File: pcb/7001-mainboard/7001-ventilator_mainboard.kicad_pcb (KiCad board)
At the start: 2 copper layers, 98.5 x 110 mm, 153 parts, among them J1 USB_B_Micro, J10 6-pin header, J11 4-pin screw terminal, J12 3-pin screw terminal, J13 2-pin screw terminal, J14 2-pin screw terminal, J15 2x10-pin header, J16 10-pin SWD header, J2 4-pin header, J3 2-pin screw terminal, J4 DNI, J5 2-pin screw terminal, J6 5V out, J7 2-pin screw terminal, J8 3-pin screw terminal, J9 Raspberry_Pi_2_3, U1 MPRLS0001PG0000SA, U10 ABPMAND001PG2A3, U11 MPVZ5010GW6U, U12 MPVZ5010GW6U, U13 ITS4142NHUMA1, U14 ITS4142NHUMA1, U2 TPD2E2U06, U3 LPC11U37FBD48-401_, U4 MCP1825S-3302E, U5 S24SE05004PDFA_DC-DC, U6 LM2937IMP-12/NOPB, U7 AD5410AREZ, U8 MPRLS0001PG0000SA, U9 ABPMAND001PG2A3, Y1 12MHz

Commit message: PCB: schematics for V2
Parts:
- removed J12: 3-pin screw terminal, Jitter_Footprints:TerminalBlock_Wurth_WR-TBL_691322110003_1x03_P3.50mm_Horizontal
- removed JP1: 5V_jumper, Connector_PinHeader_2.54mm:PinHeader_1x03_P2.54mm_Vertical
- removed R22, R23, R27, R28: 0, Resistor_SMD:R_0805_2012Metric
- removed R24, R25, R26: DNI, Resistor_SMD:R_0805_2012Metric
- removed U10: ABPMAND001PG2A3, Jitter_Footprints:ABPM+DXXX000XX0XX
- removed U12: MPVZ5010GW6U, Jitter_Footprints:MPVZ5010GW6U
- added FB1: BLM18HE601SN1D, Inductor_SMD:L_0603_1608Metric, F.Cu at (118.8, 123.8)
- added FB2: BLM18HE601SN1D, Inductor_SMD:L_0603_1608Metric, F.Cu at (102.2, 109.3)
- added H7: DNI (mounting hole), MountingHole:MountingHole_3.5mm_Pad_Via, F.Cu at (71.0, 159.0)
- added Q1: NX3020NAKV,115, Package_TO_SOT_SMD:SOT-666, F.Cu at (238.0, 176.2)
- added R44: 3.3k, Resistor_SMD:R_0805_2012Metric, F.Cu at (224.4, 181.0)
- added R45: 3.3k, Resistor_SMD:R_0805_2012Metric, F.Cu at (236.5, 170.2)
- added R46: 3.3k, Resistor_SMD:R_0805_2012Metric, F.Cu at (240.9, 167.1)
- added R47: 150, Resistor_SMD:R_0805_2012Metric, F.Cu at (117.5, 119.7)
- added R48: 2.2k, Resistor_SMD:R_0805_2012Metric, F.Cu at (119.5, 119.8)
- added R49: 150, Resistor_SMD:R_0805_2012Metric, F.Cu at (102.5, 113.5)
- added R50: 150, Resistor_SMD:R_0805_2012Metric, F.Cu at (102.5, 111.4)
- added TP6: DNI, TestPoint:TestPoint_THTPad_D1.5mm_Drill0.7mm, F.Cu at (242.2, 173.3)
- added TP7: DNI, TestPoint:TestPoint_THTPad_D1.5mm_Drill0.7mm, F.Cu at (130.5, 199.0)
- added U15: MCP4725, Package_TO_SOT_SMD:SOT-23-6, F.Cu at (122.2, 195.5)
- added U16: LD1086DT33TR, Package_TO_SOT_SMD:TO-252-2, F.Cu at (112.8, 123.5)
- C14: value 10uF -> 10uF 50V; footprint Capacitor_SMD:C_0805_2012Metric -> Capacitor_SMD:C_1210_3225Metric
- C20: value 100nF 50V -> 2.2nF
- C21: value 10uF 50V -> 100nF; footprint Capacitor_SMD:C_1210_3225Metric -> Capacitor_SMD:C_0805_2012Metric
- C23: value 10nF -> 100nF
- C24, C41: value 100nF 50V -> 10uF 50V; footprint Capacitor_SMD:C_0805_2012Metric -> Capacitor_SMD:C_1210_3225Metric
- C26: value 100nF -> 10uF 50V; footprint Capacitor_SMD:C_0805_2012Metric -> Capacitor_SMD:C_1210_3225Metric
- C27: value 10nF -> 2.2nF 50V
- C36: value 470pF -> 1nF
- C40: value 100nF -> 2.2nF
- C43: value 100nF -> 10uF
- C48: value 10nF -> 100nF 50V
- D11: value D_TVS -> D_Schottky; footprint Jitter_Footprints:WE-TVSP_TVS_DIODE -> Diode_SMD:D_SOD-123F
- D5: value D_TVS -> Green; footprint Jitter_Footprints:WE-TVSP_TVS_DIODE -> LED_SMD:LED_0805_2012Metric
- J11: value 4-pin screw terminal -> 2-pin screw terminal
- J2: value 4-pin header -> 2-pin screw terminal; footprint Connector_PinSocket_2.54mm:PinSocket_1x04_P2.54mm_Vertical -> Jitter_Footprints:TerminalBlock_Wurth_WR-TBL_691322110002_1x02_P3.50mm_Horizontal
- J4: value DNI -> 2-pin screw terminal; footprint Connector_PinHeader_2.54mm:PinHeader_1x03_P2.54mm_Vertical -> Jitter_Footprints:TerminalBlock_Wurth_WR-TBL_691322110002_1x02_P3.50mm_Horizontal
- J6: footprint Connector_PinHeader_2.54mm:PinHeader_1x02_P2.54mm_Vertical -> Connector_PinHeader_2.54mm:PinHeader_1x05_P2.54mm_Vertical
- J7: value 2-pin screw terminal -> 6-pin FFC connector; footprint Jitter_Footprints:TerminalBlock_Wurth_WR-TBL_691322110002_1x02_P3.50mm_Horizontal -> Jitter_Footprints:Hirose_FH12-6S-0.5SH_1x06-1MP_P0.50mm_Horizontal
- J8: value 3-pin screw terminal -> 2-pin screw terminal; footprint Jitter_Footprints:TerminalBlock_Wurth_WR-TBL_691322110003_1x03_P3.50mm_Horizontal -> Jitter_Footprints:TerminalBlock_Wurth_WR-TBL_691322110004_1x04_P3.50mm_Horizontal
- R10: value 10k -> 68k
- R11: value 0 -> 1k5
- R12: value 10k -> 1k5
- R13, R33: value 0 -> 100k
- R14: value DNI -> 100k
- R15: value 150 -> 10k
- R18: value 0 -> 10k
- R19, R37: value DNI -> 3.3k
- R21: value 100k -> 4.7k
- R31: value 3.3k -> 68k
- R32: value 10k -> 4.7k
- R35: value 4.7k -> 10k
- R8, R9: value 1k5 -> 0
- U6: value LM2937IMP-12/NOPB -> MCP4725; footprint Package_TO_SOT_SMD:SOT-223-3_TabPin2 -> Package_TO_SOT_SMD:SOT-23-6
- U7: value AD5410AREZ -> ITS4142NHUMA1; footprint Jitter_Footprints:TSSOP-24-1EP_4.4x7.8mm_P0.65mm -> Package_TO_SOT_SMD:SOT-223
- U9: value ABPMAND001PG2A3 -> ABPDXXX000XXAX5; footprint Jitter_Footprints:ABPM+DXXX000XX0XX -> Jitter_Footprints:ABPDXXX000XX0XX
- moved R12 165.1 mm to (232.1, 170.5), turned to 0 degrees
- moved R11 154.5 mm to (236.5, 167.2), turned to 0 degrees
- moved R9 153.7 mm to (233.8, 173.4), turned to 0 degrees
- moved R15 151.4 mm to (220.0, 179.8), turned to 0 degrees
- moved R8 147.1 mm to (229.4, 173.4), turned to 0 degrees
- moved R14 145.7 mm to (215.1, 187.4)
- moved C24 144.1 mm to (227.9, 160.6), turned to 0 degrees
- moved C21 142.0 mm to (225.0, 172.2), turned to 0 degrees
- moved C1 134.8 mm to (241.6, 162.9)
- moved R35 134.1 mm to (229.4, 176.4), turned to 0 degrees
- moved R18 132.9 mm to (215.1, 184.5), turned to 0 degrees
- moved C20 132.1 mm to (220.0, 182.8)
- moved R10 128.8 mm to (225.0, 178.1), turned to 0 degrees
- moved R37 127.2 mm to (215.1, 190.4)
- moved C15 124.9 mm to (219.5, 185.7), turned to 0 degrees
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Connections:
- net /24V_SW1_OUT renamed /EXHALE_VALVE
- net /24V_SW2_OUT renamed /INHALE_VALVE
- net /pressure_sensor/MPVZ5010_1_OUT renamed /pressure_sensor/MPVZ5010_OUT
- net /switch_1_out renamed /EXHALE_PWM
- net /switch_2_out renamed /INHALE_PWM
- C1 pad 1: /USB_VBUS -> +5V
- C11 pad 1: /DCDC_5V -> +5V
- C14 pad 1: +3V3 -> +24V
- C15 pad 1: +3V3 -> /POWER_STATUS
- C16 pad 1: /DCDC_5V -> +5V
- C19 pad 1: +24V -> Net-(C19-Pad1)
- C20 pad 1: +24V -> /A_MFC_FEEDBACK_O2
- C21 pad 1: +24V -> /USER_SWITCH
- C23 pad 1: +24V -> +5V
- C23 pad 2: Net-(C23-Pad2) -> GND
- C26 pad 1: Net-(C26-Pad1) -> +24V
- C27 pad 1: /A_PREG_PRESSURE -> /EXTRA_VALVE
- C35 pad 1: /A_PRESSURE_1 -> /A_PSENSE_3
- C36 pad 1: /pressure_sensor/MPVZ5010_2_OUT -> Net-(C36-Pad1)
- C37 pad 1: /A_PRESSURE_2 -> /A_MFC_PRESSURE
- C38 pad 1: +12V -> /V_flow_heater
- C39 pad 1: +12V -> /V_flow_heater
- C40 pad 1: +5V -> /A_MFC_FEEDBACK_AIR
- C41 pad 1: +12V -> +24V
- C43 pad 1: /A_FLOW -> +3V3
- C48 pad 1: +24V -> /V_flow_3v3
- C48 pad 2: Net-(C48-Pad2) -> GND
- D11 pad 1: GND -> /EXTRA_VALVE
- D11 pad 2: +24V -> GND
- D5 pad 2: /I_PREG_SETPOINT -> Net-(D5-Pad2)
- FL1 pad 1: Net-(C46-Pad1) -> Net-(C46-Pad2)
- FL1 pad 2: Net-(C46-Pad2) -> Net-(C46-Pad1)
- FL1 pad 3: Net-(C47-Pad1) -> GND
- FL1 pad 4: GND -> Net-(C47-Pad1)
- J11 pad 2: +5V -> Net-(J11-Pad2)
- J11 pad 3: /I2C_SDA -> /MFC_SETPOINT_AIR
- J11 pad 4: /I2C_SCL -> +24V
- J15 pad 2: /RPI_IO_3 -> /RPI_IO_2
- J15 pad 4: /RPI_IO_2 -> /RPI_IO_1
- J15 pad 6: /RPI_IO_1 -> /~ISP~
- J2 pad 1: GND -> Net-(J2-Pad1)
- J2 pad 2: /SWCLK -> Net-(J2-Pad2)
- J3 pad 2: +12V -> Net-(J3-Pad2)
- J4 pad 2: /~RESET~ -> /EXTRA_VALVE
- J5 pad 1: Net-(C46-Pad1) -> Net-(C46-Pad2)
- J5 pad 2: Net-(C46-Pad2) -> Net-(C46-Pad1)
- J6 pad 2: +5V -> (no net)
- J7 pad 1: GND -> /V_flow_3v3
- J7 pad 2: +24V -> GND
- J8 pad 2: /I_PREG_FEEDBACK -> Net-(J8-Pad2)
- J8 pad 3: /I_PREG_SETPOINT -> /MFC_SETPOINT_O2
- J9 pad 11: (no net) -> /RPI_~ISP~
- J9 pad 36: /~RESET~ -> /RPI_~RST~
- J9 pad 40: /RPI_IO_3 -> (no net)
- J9 pad 5: (no net) -> /RPI_ON_OFF
- R1 pad 1: /A_PRESSURE_1 -> /A_PSENSE_3
- R10 pad 1: /PREG_OK -> /A_MFC_FEEDBACK_O2
- R10 pad 2: +3V3 -> Net-(J8-Pad2)
- R11 pad 1: GND -> Net-(J2-Pad2)
- R11 pad 2: Net-(R11-Pad2) -> +3V3
- R12 pad 1: /A_PREG_PRESSURE -> Net-(J2-Pad1)
- R12 pad 2: Net-(R12-Pad2) -> /POWER_STATUS
- R13 pad 1: Net-(R12-Pad2) -> GND
- R13 pad 2: /I_PREG_FEEDBACK -> /A_MFC_PRESSURE
- R14 pad 1: /A_PREG_PRESSURE -> GND
- R14 pad 2: GND -> /A_MFC_FEEDBACK_O2
- R15 pad 1: GND -> +3V3
- R15 pad 2: Net-(R12-Pad2) -> Net-(J3-Pad2)
- R18 pad 1: +3V3 -> Net-(J3-Pad2)
- R18 pad 2: /V_PU -> /USER_SWITCH
- R19 pad 1: /V_PU -> Net-(D5-Pad2)
- R19 pad 2: +5V -> /EXTRA_VALVE
- R2 pad 1: /A_PRESSURE_2 -> /A_MFC_PRESSURE
- R2 pad 2: /pressure_sensor/MPVZ5010_2_OUT -> Net-(C36-Pad1)
- R20 pad 2: /A_PRESSURE_1 -> /A_PSENSE_3
- R21 pad 2: /A_PRESSURE_2 -> /USB_VBUS
- R31 pad 1: GND -> /A_MFC_FEEDBACK_AIR
- R31 pad 2: /A_FLOW -> Net-(J11-Pad2)
- R32 pad 1: /A_FLOW -> GND
- R32 pad 2: Net-(J12-Pad3) -> /EXTRA_PWM
- R33 pad 1: /DCDC_5V -> GND
- R33 pad 2: +5V -> /A_MFC_FEEDBACK_AIR
- R35 pad 1: GND -> /~ISP~
- R35 pad 2: /PREG_CLEAR -> +3V3
- R37 pad 1: Net-(R37-Pad1) -> /I2C_3V3_SCL
- R37 pad 2: GND -> +3V3
- R7 pad 2: /DCDC_5V -> +5V
- R8 pad 1: /I2C_SCL -> /~RESET~
- R8 pad 2: /V_PU -> /RPI_~RST~
- R9 pad 1: /I2C_SDA -> /~ISP~
- R9 pad 2: /V_PU -> /RPI_~ISP~
- TP2 pad 1: /A_PRESSURE_1 -> /A_PSENSE_3
- TP3 pad 1: /A_PRESSURE_2 -> /A_MFC_PRESSURE
- U1 pad 12: Net-(R22-Pad2) -> +3V3
- U3 pad 10: (no net) -> /LED_STATUS
- U3 pad 11: /UART_RX -> /USER_SWITCH
- U3 pad 12: /UART_TX -> /POWER_STATUS
- U3 pad 14: +3V3 -> /USB_VBUS
- U3 pad 15: /I2C_SCL -> /I2C_3V3_SCL
- U3 pad 16: /I2C_SDA -> /I2C_3V3_SDA
- U3 pad 23: /PREG_CLEAR -> /PSENSE_2_SPI_~CS~
- U3 pad 24: /PREG_OK -> (no net)
- U3 pad 25: /PREG_SPI_~CS~ -> (no net)
- U3 pad 26: /PREG_SPI_MISO -> (no net)
- U3 pad 32: /A_PREG_PRESSURE -> /A_PSENSE_3
- U3 pad 33: /A_FLOW -> /A_MFC_PRESSURE
- U3 pad 34: /A_PRESSURE_2 -> /A_MFC_FEEDBACK_AIR
- U3 pad 35: /A_PRESSURE_1 -> /A_MFC_FEEDBACK_O2
- U3 pad 36: /MCU_IO_1 -> /EXTRA_PWM
- U3 pad 38: /PREG_SPI_MOSI -> /MCU_IO_3
- U3 pad 40: /PSENSE_2_SPI_~CS~ -> /MCU_IO_1
- U3 pad 43: /PREG_SPI_CLK -> /MCU_IO_4
- U3 pad 45: /LED_STATUS -> /RPI_ON_OFF
- U3 pad 46: /MCU_IO_4 -> /UART_RX
- U3 pad 47: /MCU_IO_3 -> /UART_TX
- U3 pad 9: (no net) -> GND
- U5 pad 6: /DCDC_5V -> +5V
- U6 pad 1: +24V -> /MFC_SETPOINT_O2
- U6 pad 3: +12V -> +5V
- U7 pad 1: GND -> /EXTRA_VALVE
- U7 pad 2: +3V3 -> GND
- U7 pad 3: /PREG_OK -> /EXTRA_PWM
- U7 pad 4: GND -> +24V
- U8 pad 12: Net-(R23-Pad2) -> +3V3
- U9 pad 2: Net-(R22-Pad2) -> (no net)
- U9 pad 3: /PSENSE_1_DATA_READY -> Net-(C36-Pad1)
- U9 pad 4: Net-(U9-Pad4) -> (no net)
- U9 pad 5: /pressure_sensor/P_SDA -> (no net)
- U9 pad 6: /pressure_sensor/P_SCL -> +5V
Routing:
- net +3V3: track 295.0 -> 0.47 mm, vias 9 -> 0
- net +5V: track 255.1 -> 24.8 mm, vias 8 -> 0
- net /I2C_SDA: track 126.9 -> 0.00 mm, vias 4 -> 0
- net /I2C_SCL: track 126.4 -> 0.00 mm, vias 6 -> 0
- net +24V: track 163.9 -> 49.7 mm
- net /A_PREG_PRESSURE: track 102.0 -> 0.00 mm, vias 2 -> 0
- net GND: track 271.6 -> 170.9 mm, vias 166 -> 48
- net /PSENSE_SPI_MISO: track 99.7 -> 0.00 mm, vias 6 -> 0
- net /EXHALE_PWM: track 96.0 -> 3.03 mm, vias 4 -> 0
- net /~RESET~: track 91.5 -> 0.00 mm, vias 2 -> 0
- net /PSENSE_2_DATA_READY: track 87.6 -> 0.00 mm, vias 5 -> 0
- net /PSENSE_SPI_MOSI: track 87.0 -> 0.00 mm, vias 4 -> 0
- net /A_FLOW: track 86.3 -> 0.00 mm, vias 2 -> 0
- net /PSENSE_RESET: track 88.1 -> 1.97 mm, vias 4 -> 1
- net /PREG_SPI_MOSI: track 83.3 -> 0.00 mm, vias 4 -> 0
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- removed copper zone on F.Cu, net +24V
- removed copper zone on F.Cu, net +5V
- removed copper zone on F.Cu, net GND

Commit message: Update schematics (PSU connector) + BOM
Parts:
- removed J2: 2-pin screw terminal, Jitter_Footprints:TerminalBlock_Wurth_WR-TBL_691322110002_1x02_P3.50mm_Horizontal
- added C50: 100nF, Capacitor_SMD:C_0805_2012Metric, F.Cu at (191.8, 135.5)
- added R22: 1k5, Resistor_SMD:R_0805_2012Metric, F.Cu at (191.8, 138.4)
- added R23: 1k5, Resistor_SMD:R_0805_2012Metric, F.Cu at (196.2, 135.5)
- J11, J8: footprint Jitter_Footprints:TerminalBlock_Wurth_WR-TBL_691322110004_1x04_P3.50mm_Horizontal -> Jitter_Footprints:TerminalBlock_Wurth_WR-TBL_691322110005_1x05_P3.50mm_Horizontal
- J5: footprint Jitter_Footprints:TerminalBlock_Wurth_WR-TBL_691322110002_1x02_P3.50mm_Horizontal -> Jitter_Footprints:TerminalBlock_Wurth_WR-TBL_691322110008_1x08_P3.50mm_Horizontal
- moved J3 43.2 mm to (158.5, 162.5)
- moved J1 10.5 mm to (162.3, 172.2)
- moved U2 10.5 mm to (156.3, 172.4)
- moved J5 3.65 mm to (158.5, 147.0)
- moved D4 1.69 mm to (154.2, 139.5)
- moved J8 1.00 mm to (133.5, 203.5)
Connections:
- C15 pad 1: /POWER_STATUS -> /POWER_STATUS_DISCHARGING
- J11 pad 4: +24V -> GND
- J5 pad 1: Net-(C46-Pad2) -> GND
- J5 pad 2: Net-(C46-Pad1) -> GND
- J8 pad 4: +24V -> GND
- R11 pad 1: Net-(J2-Pad2) -> Net-(J5-Pad6)
- R12 pad 1: Net-(J2-Pad1) -> Net-(J5-Pad5)
- R12 pad 2: /POWER_STATUS -> /POWER_STATUS_DISCHARGING
- U3 pad 12: /POWER_STATUS -> /POWER_STATUS_FAIL
- U3 pad 13: /PSENSE_RESET -> /POWER_STATUS_DISCHARGING
- U3 pad 24: (no net) -> /PSENSE_RESET

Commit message: PCB: layout in progress
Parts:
- removed R11: 1k5, Resistor_SMD:R_0805_2012Metric
- moved R42 119.9 mm to (98.1, 173.2)
- moved R43 119.9 mm to (99.0, 178.4)
- moved D10 119.9 mm to (101.8, 178.2)
- moved D9 119.9 mm to (99.1, 175.2)
- moved C24 108.9 mm to (126.2, 199.8), turned to 180 degrees
- moved TP6 105.2 mm to (139.4, 196.2)
- moved C1 101.0 mm to (146.0, 195.6), turned to 270 degrees
- moved TP2 100.0 mm to (92.2, 150.9)
- moved R10 88.1 mm to (139.4, 199.2), turned to 270 degrees
- moved C20 84.6 mm to (136.8, 198.6), turned to 180 degrees
- moved TP5 81.3 mm to (97.3, 137.1)
- moved R41 81.3 mm to (94.8, 137.6)
- moved TP1 81.3 mm to (92.4, 137.2)
- moved D8 81.3 mm to (94.8, 141.2)
- moved R14 79.4 mm to (136.8, 200.5)
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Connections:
- J5 pad 8: Net-(J5-Pad8) -> Net-(J5-Pad6)
- J7 pad MP: (no net) -> GND
- R23 pad 1: Net-(J5-Pad8) -> Net-(J5-Pad6)
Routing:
- net +24V: track 49.7 -> 181.4 mm, vias 0 -> 2
- net +3V3: track 0.47 -> 62.2 mm
- net /I2C_3V3_SDA: track 0.00 -> 60.4 mm, vias 0 -> 2
- net /I2C_3V3_SCL: track 0.00 -> 57.4 mm, vias 0 -> 2
- net GND: track 170.9 -> 223.5 mm, vias 48 -> 71
- net Net-(J5-Pad6): track 0.00 -> 38.6 mm
- net Net-(J5-Pad7): track 0.00 -> 34.9 mm
- net /RPI_~RST~: track 51.5 -> 85.4 mm
- net Net-(J5-Pad5): track 0.00 -> 32.4 mm
- net /RPI_IO_1: track 53.7 -> 86.1 mm
- net /RPI_IO_2: track 48.4 -> 79.8 mm
- net /RPI_ON_OFF: track 32.9 -> 62.0 mm
- net /RPI_~ISP~: track 28.9 -> 55.9 mm
- net /RPI_TX: track 39.6 -> 66.2 mm
- net /RPI_RX: track 36.4 -> 62.0 mm
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- added copper zone on F.Cu, net +5V
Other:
- board size 98.5 x 110 mm -> 99 x 110.5 mm

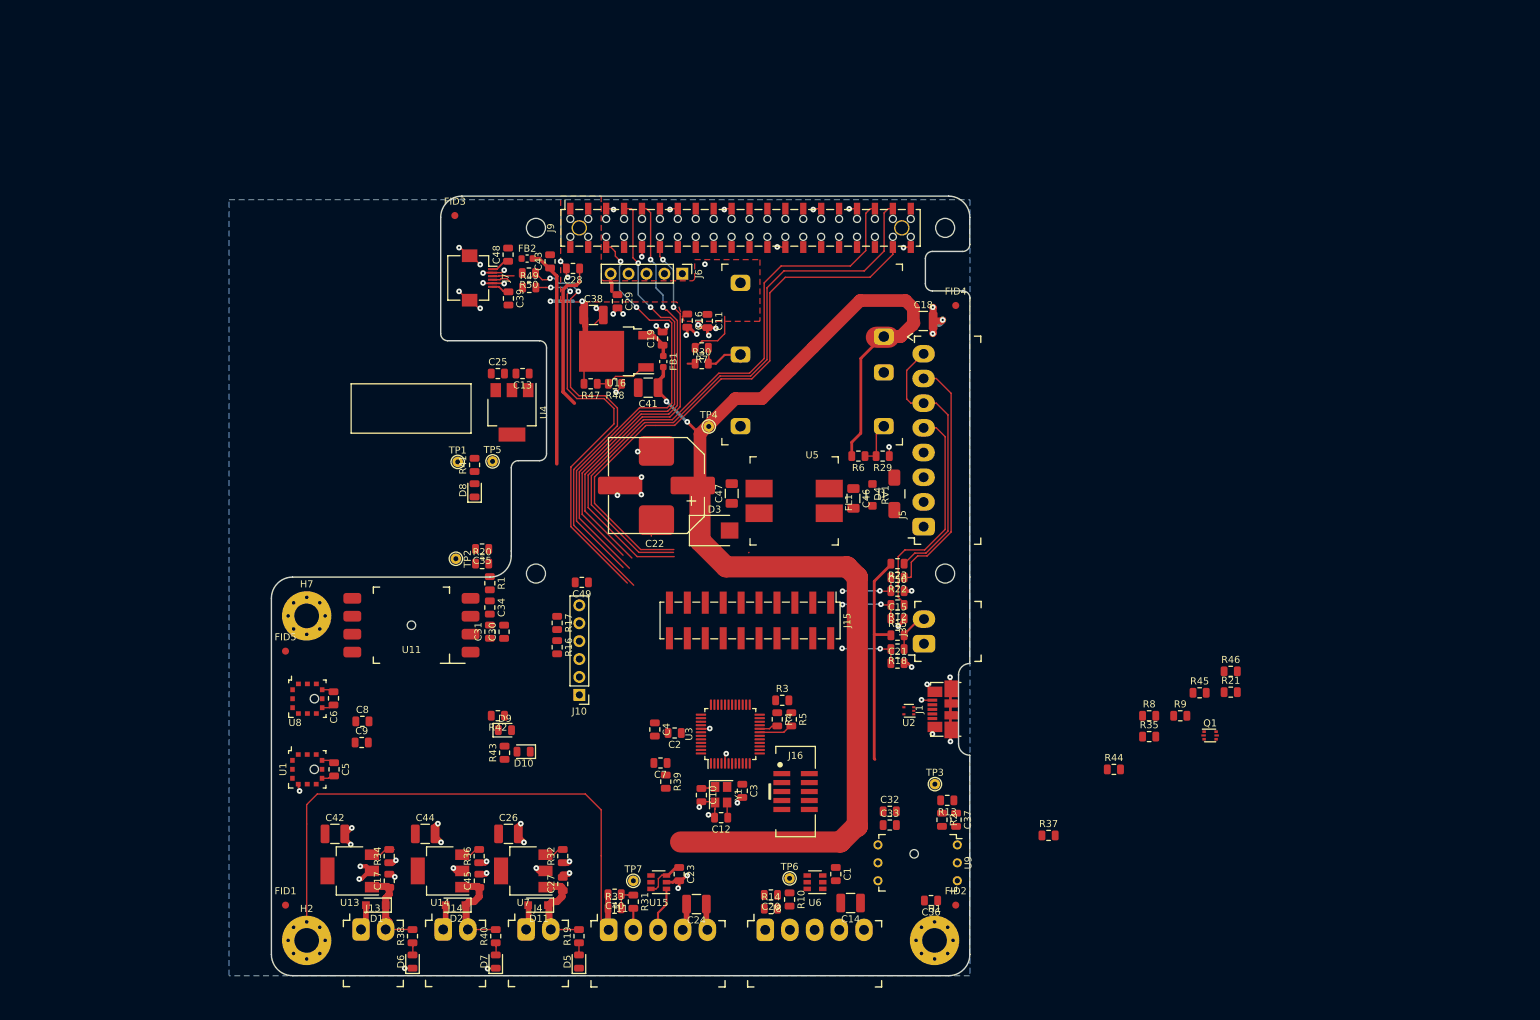
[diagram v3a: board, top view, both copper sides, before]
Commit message: PCB layout: position of components near-final
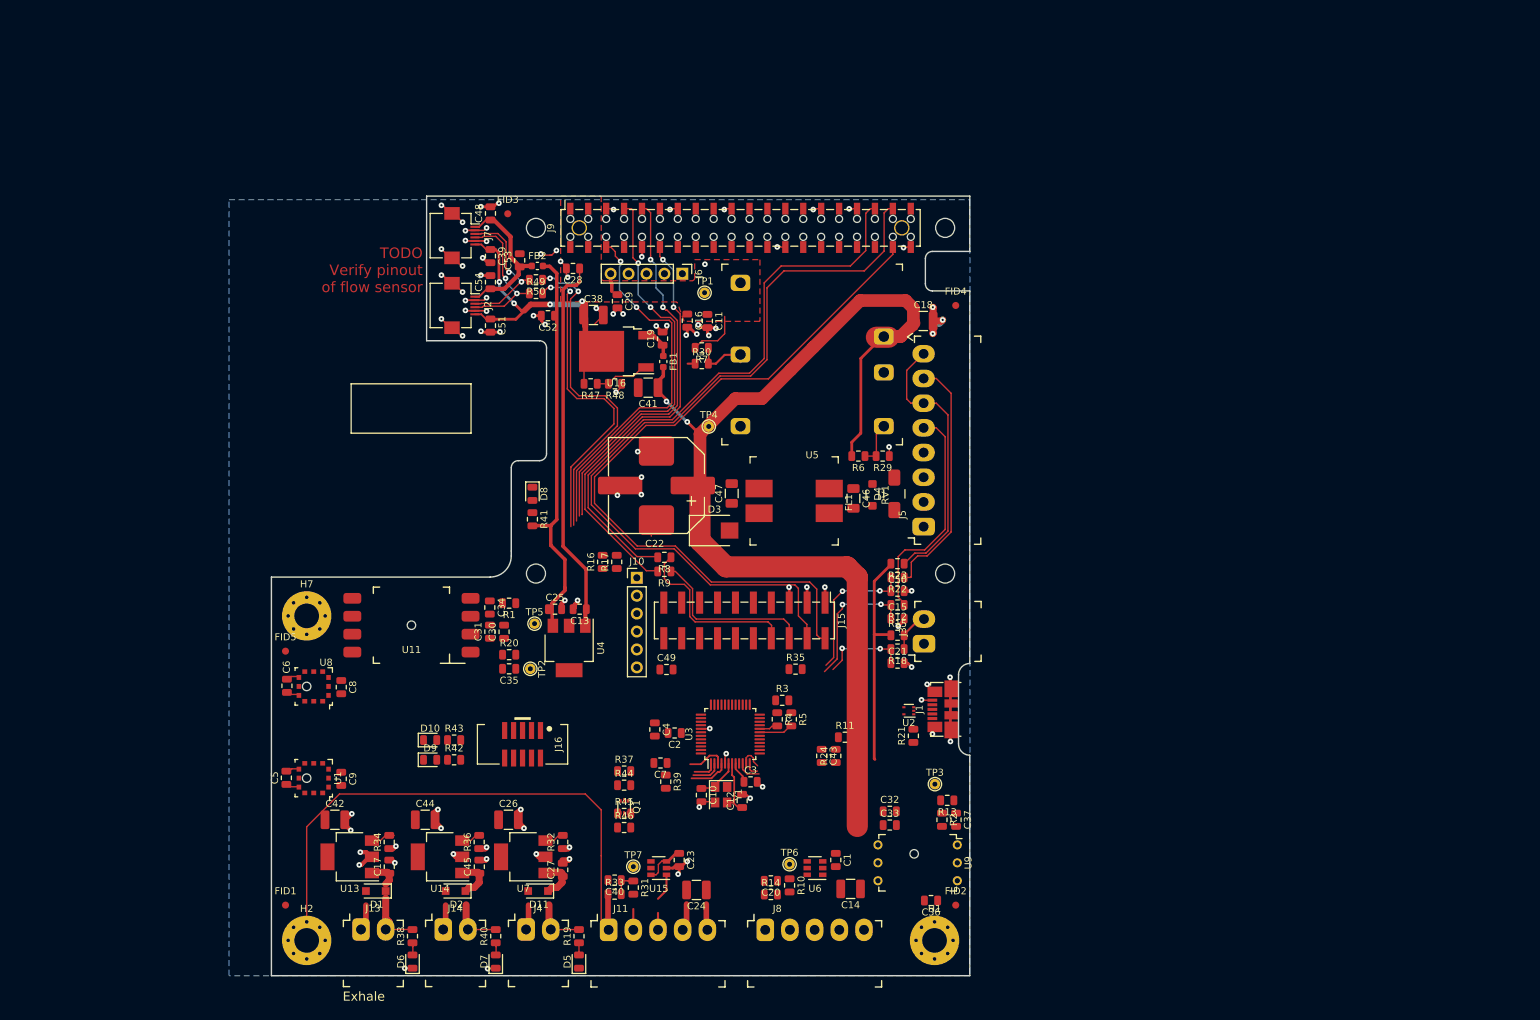
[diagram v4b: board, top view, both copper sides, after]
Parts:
- added C51: 100nF 50V, Capacitor_SMD:C_0805_2012Metric, F.Cu at (97.0, 117.8)
- added C52: 1uF, Capacitor_SMD:C_0805_2012Metric, F.Cu at (105.2, 116.5)
- added C53: 10uF, Capacitor_SMD:C_0805_2012Metric, F.Cu at (101.2, 108.6)
- added C54: 100nF 50V, Capacitor_SMD:C_0805_2012Metric, F.Cu at (97.0, 111.7)
- added J2: 6-pin FFC connector, Jitter_Footprints:Hirose_FH12-6S-0.5SH_1x06-1MP_P0.50mm_Horizontal, F.Cu at (93.0, 115.0)
- added R11: 10k, Resistor_SMD:R_0805_2012Metric, F.Cu at (147.3, 176.2)
- added R24: 1k5, Resistor_SMD:R_0805_2012Metric, F.Cu at (146.0, 178.8)
- C43: value 10uF -> 100nF
- R47: value 150 -> 150 1%
- R48: value 2.2k -> 2.32k 1%
- moved R46 88.8 mm to (116.0, 189.0)
- moved Q1 83.7 mm to (116.0, 186.1), turned to 270 degrees
- moved R45 83.3 mm to (116.0, 187.0)
- moved C43 80.0 mm to (144.0, 178.8), turned to 270 degrees
- moved R9 75.9 mm to (121.7, 152.7), turned to 180 degrees
- moved R8 72.3 mm to (121.7, 150.7), turned to 180 degrees
- moved R44 69.5 mm to (116.0, 183.0)
- moved R37 60.8 mm to (116.0, 181.0)
- moved R35 51.0 mm to (140.3, 166.6)
- moved R21 45.4 mm to (157.0, 176.0), turned to 90 degrees
- moved TP1 42.4 mm to (127.4, 113.2)
- moved J16 39.3 mm to (101.6, 177.2), turned to 270 degrees
- moved C13 34.4 mm to (109.7, 158.1)
- moved C25 34.4 mm to (106.2, 158.1)
- moved U4 34.4 mm to (108.2, 163.6)
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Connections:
- C43 pad 1: +3V3 -> /BATT_LEVEL
- U3 pad 17: (no net) -> /LED_ERROR
- U3 pad 42: /LED_ERROR -> /BATT_LEVEL
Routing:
- net GND: track 223.5 -> 256.8 mm, vias 71 -> 94
- net +5V: track 37.4 -> 69.7 mm
- net /~RESET~: track 0.00 -> 30.8 mm
- net /~ISP~: track 0.00 -> 29.5 mm
- net +3V3: track 62.2 -> 90.8 mm
- net /RPI_IO_1: track 86.1 -> 113.4 mm
- net +24V: track 181.4 -> 155.5 mm
- net /RPI_IO_2: track 79.8 -> 104.6 mm
- net /V_flow_heater: track 19.6 -> 44.4 mm, vias 2 -> 4
- net /V_flow_3v3: track 2.37 -> 21.1 mm
- net /FLOW_I2C_SCL: track 2.68 -> 20.9 mm, vias 0 -> 2
- net /FLOW_I2C_SDA: track 3.07 -> 20.9 mm, vias 0 -> 2
- net /I2C_3V3_SDA: track 60.4 -> 46.6 mm
- net /POWER_STATUS_FAIL: track 9.31 -> 22.8 mm
- net /I2C_3V3_SCL: track 57.4 -> 45.7 mm
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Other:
- outline, holes or cut-outs redrawn
- board text added: "Exhale"
- board text added: "TODO Verify pinout of flow sensor"

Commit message: PCB layout: final locations and BOM (?)
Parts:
- J5: footprint Jitter_Footprints:TerminalBlock_Wurth_WR-TBL_691322110008_1x08_P3.50mm_Horizontal -> Jitter_Footprints:TerminalBlock_Wurth_WR-TBL_691321100005_1x05_P3.50mm_Vertical
- moved D3 2.82 mm to (130.1, 149.4), turned to 90 degrees
- moved J5 2.45 mm to (160.8, 145.5)
- moved D4 2.15 mm to (153.8, 143.8)
- moved RV1 2.08 mm to (150.8, 143.9)
- moved C47 1.75 mm to (131.2, 143.4)
- moved C46 1.56 mm to (148.3, 143.9)
- moved R23 1.55 mm to (154.8, 150.1)
- moved FL1 0.89 mm to (139.7, 143.5)
- moved TP4 0.88 mm to (127.4, 132.8)
- moved U5 0.40 mm to (142.2, 122.0)
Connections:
- net Net-(C47-Pad1) renamed /24_CHOKE
- C46 pad 1: Net-(C46-Pad1) -> /PWR+
- C46 pad 2: Net-(C46-Pad2) -> /PWR-
- D4 pad 1: Net-(C46-Pad2) -> /PWR-
- D4 pad 2: Net-(C46-Pad1) -> /PWR+
- FL1 pad 1: Net-(C46-Pad2) -> /PWR-
- FL1 pad 2: Net-(C46-Pad1) -> /PWR+
- J5 pad 1: GND -> /PWR-
- J5 pad 2: GND -> /PWR+
- J5 pad 3: Net-(C46-Pad2) -> /UPS_3V3_PU
- J5 pad 4: Net-(C46-Pad1) -> /UPS_DISCHG
- J5 pad 5: Net-(J5-Pad5) -> /UPS_FAIL
- R12 pad 1: Net-(J5-Pad5) -> /UPS_DISCHG
- R22 pad 1: Net-(J5-Pad7) -> /UPS_FAIL
- R23 pad 1: Net-(J5-Pad6) -> /UPS_3V3_PU
- RV1 pad 1: Net-(C46-Pad1) -> /PWR+
- RV1 pad 2: Net-(C46-Pad2) -> /PWR-
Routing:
- net Net-(J5-Pad6): track 38.6 -> 0.00 mm
- net Net-(J5-Pad7): track 34.9 -> 0.00 mm
- net Net-(J5-Pad5): track 32.4 -> 0.00 mm
- net /UPS_DISCHG: track 0.00 -> 30.8 mm
- net /UPS_FAIL: track 0.00 -> 29.6 mm
- net /UPS_3V3_PU: track 0.00 -> 18.9 mm
- net /I2C_3V3_SCL: track 45.7 -> 54.6 mm
- net /I2C_3V3_SDA: track 46.6 -> 55.2 mm
- net /RPI_ON_OFF: track 52.7 -> 61.1 mm
- net /RPI_RX: track 53.8 -> 61.5 mm
- net /RPI_TX: track 55.8 -> 62.9 mm
- net /RPI_IO_2: track 104.6 -> 110.0 mm
- net +3V3: track 90.8 -> 92.9 mm
- net Net-(D8-Pad2): track 0.00 -> 1.88 mm
- net /RPI_IO_1: track 113.4 -> 112.0 mm
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- added copper zone on F.Cu, net /24_CHOKE
- added copper zone on F.Cu, net /PWR+
- added copper zone on F.Cu, net /PWR-
- added copper zone on F.Cu, net GND
